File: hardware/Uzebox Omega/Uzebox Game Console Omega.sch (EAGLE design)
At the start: 81 parts, among them CON1 USBSERIALSMD, IC1 MCP1700, IC2 7805T, U5 DC IN, U6 23LC1024, X1 A/V

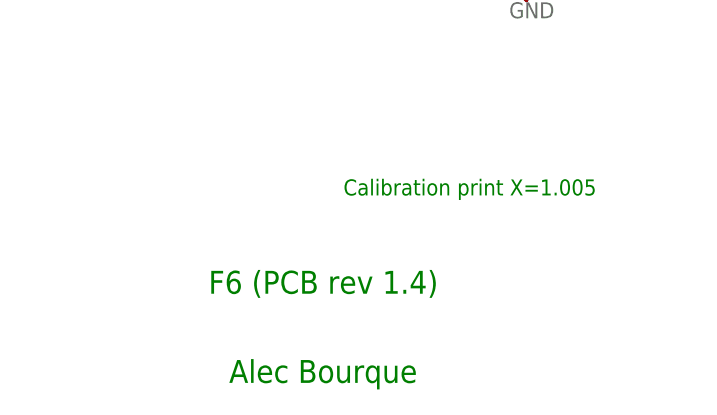
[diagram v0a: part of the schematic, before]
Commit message: Rename Uzbox F6 to Uzebox Omega
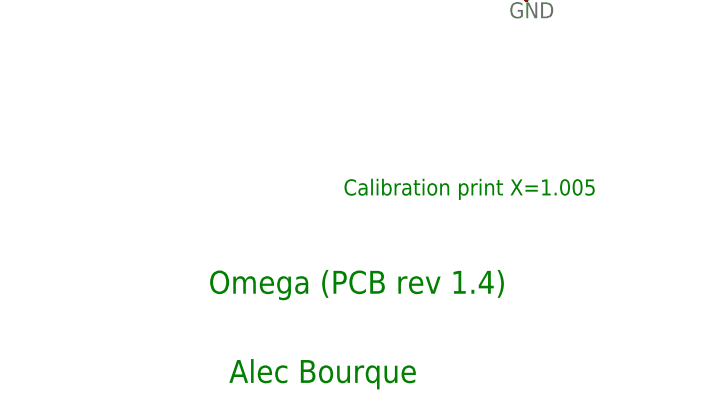
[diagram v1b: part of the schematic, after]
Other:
- note added: "Omega (PCB rev 1.4)"
- note removed: "F6 (PCB rev 1.4)"
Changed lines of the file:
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@@
 <text x="269.24" y="-30.48" size="1.778" layer="91">Calibration print X=1.005</text>
 <text x="-66.04" y="-25.4" size="1.778" layer="91">Video DAC design and SD voltage dividers contributed by Clay Cowgill.</text>
-<text x="254.254" y="-41.402" size="2.54" layer="91">F6 (PCB rev 1.4)</text>
+<text x="254.254" y="-41.402" size="2.54" layer="91">Omega (PCB rev 1.4)</text>
 <text x="218.694" y="153.162" size="1.778" layer="91">Optional Uzenet Interface</text>
 <text x="-66.04" y="-33.02" size="1.778" layer="91">Added Mini-DIN SCART connector and some cleanup by Thorsten Erdmann (Bluescreen@trektech.de)</text>

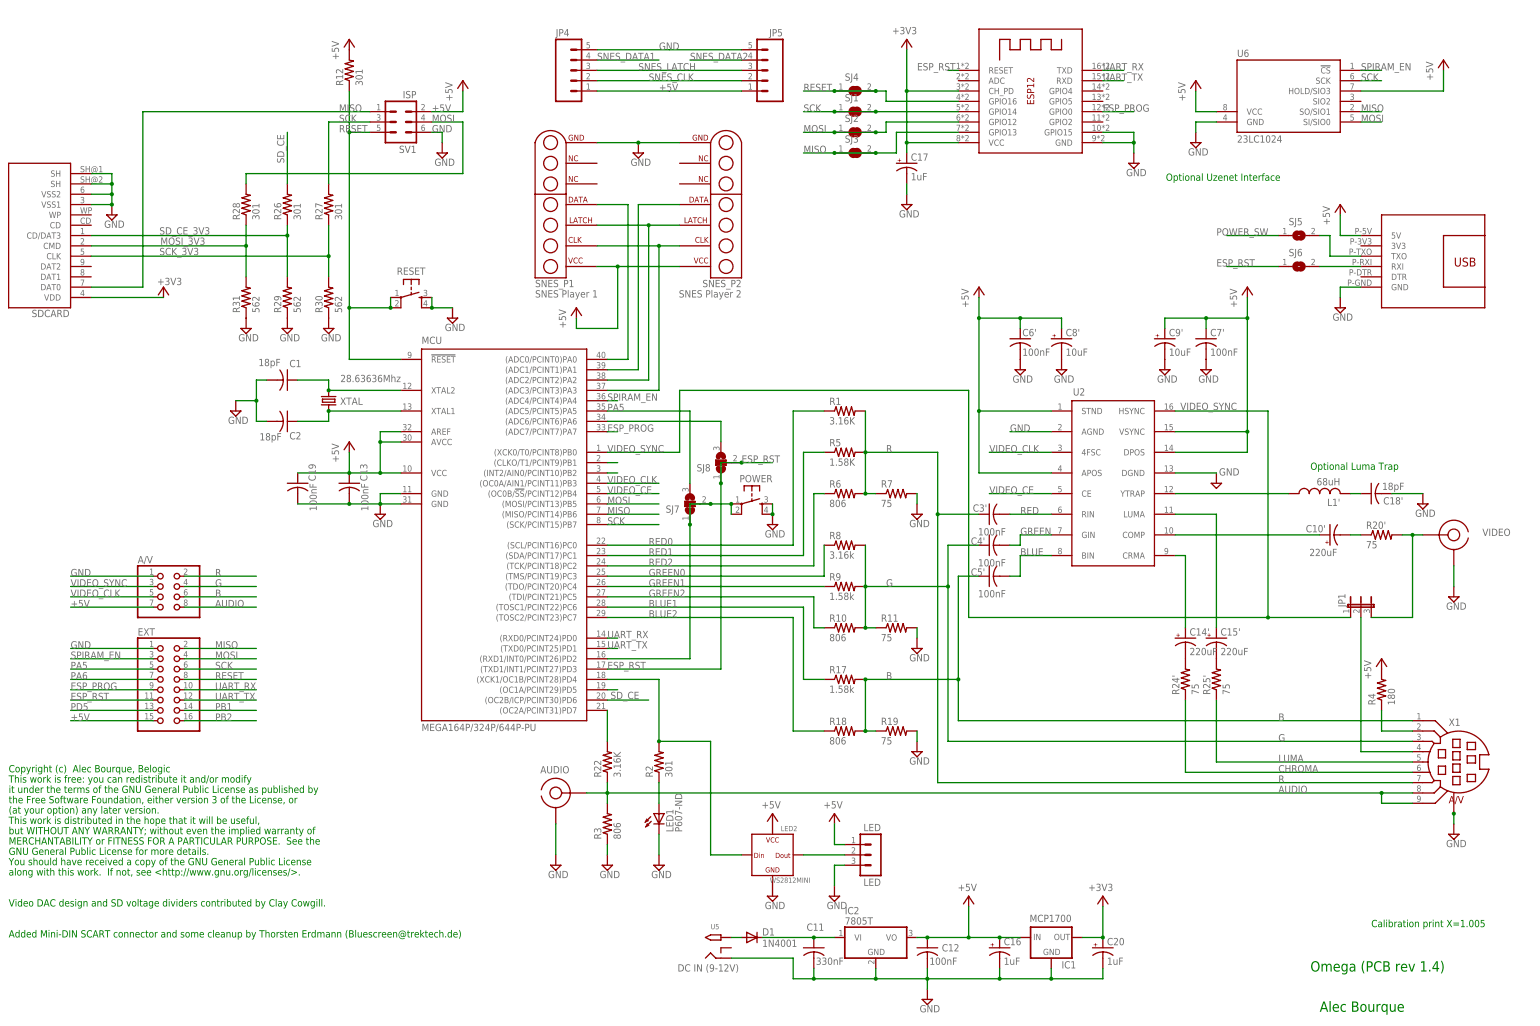
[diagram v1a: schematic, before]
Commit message: Modified schematic for better readability and corrected silkscreen version
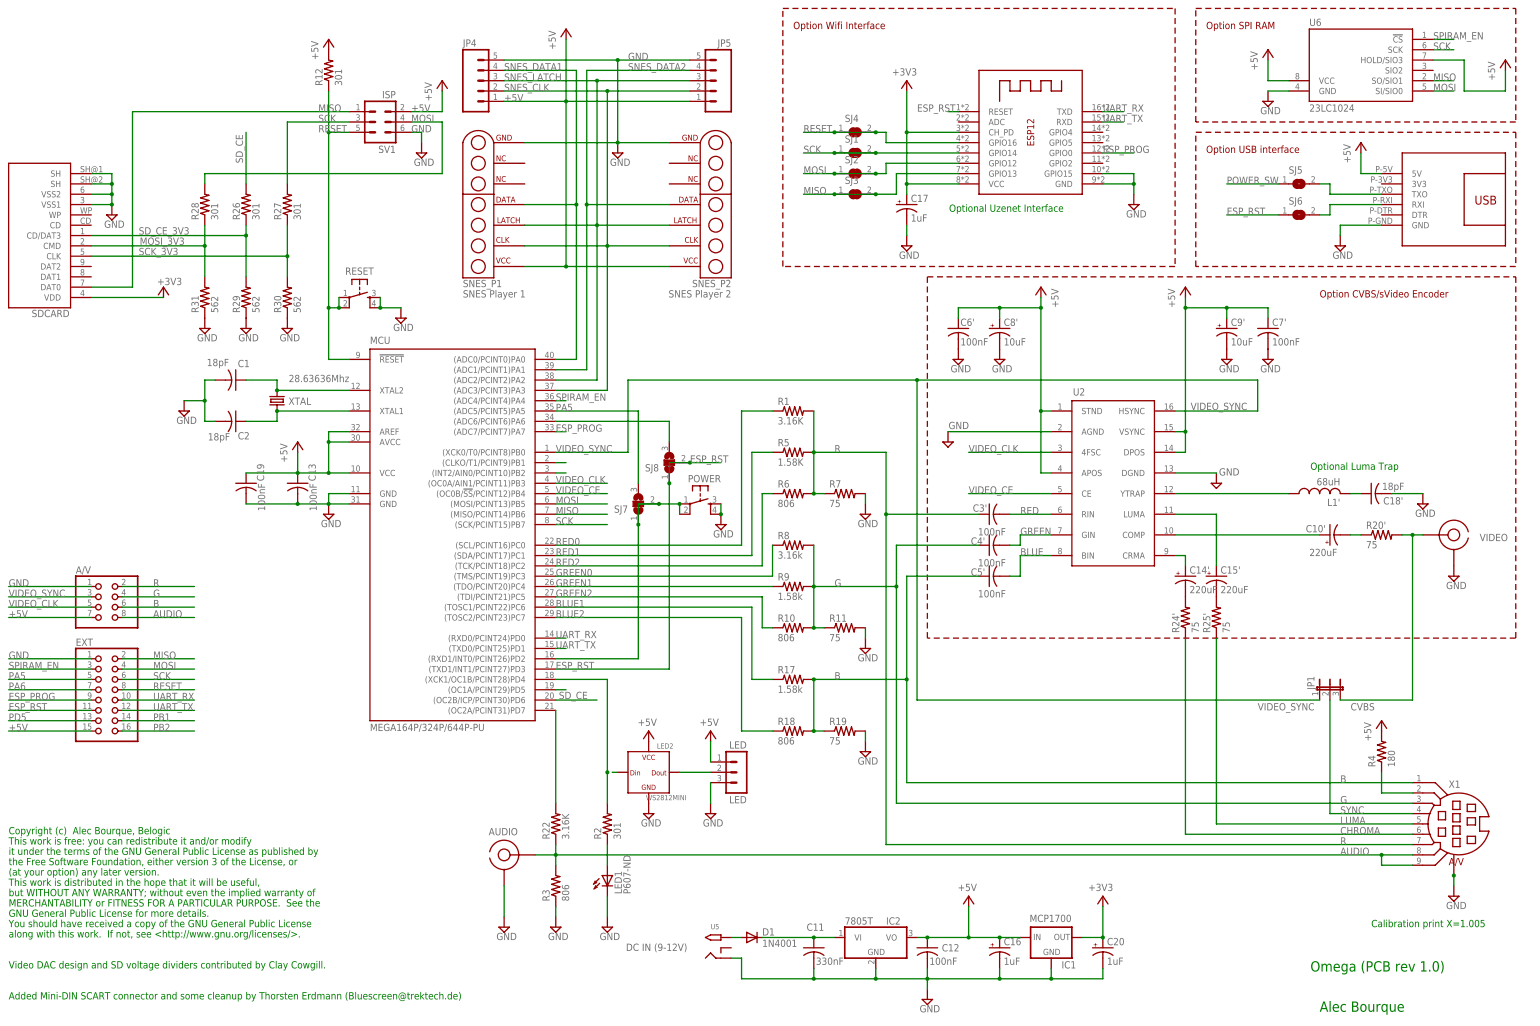
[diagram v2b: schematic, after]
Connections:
- net N$17 renamed SYNC
- net N$8 renamed CVBS
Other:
- note added: "Omega (PCB rev 1.0)"
- note added: "Option CVBS/sVideo Encoder"
- note added: "Option SPI RAM"
- note added: "Option USB interface"
- note added: "Option Wifi Interface"
- note removed: "Omega (PCB rev 1.4)"
- moved on the sheet: A/V, AUDIO, C1, C13, C14', C15', C17, C19, C2, C6', C7', C8'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
